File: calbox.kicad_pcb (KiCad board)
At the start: 2 copper layers, 101.6 x 76.2 mm, 80 parts, among them P1 BNC, P2 CONN_01X01, P3 CONN_01X01, Q1 Q_NPN_BEC, SW1 SW_Rotary12, SW2 SW_Rotary12, SW3 SW_SPDT, SW4 SW_Rotary12, SW5 SW_DPST_NKK_M2021, U1 74LVC161, U10 74LVC161, U11 74LVC74, U12 74LVC14, U13 LM317_SOT223_4pin, U14 LM317_SOT223_4pin, U2 74LVC161, U3 74LVC161, U4 74LVC161, U5 74LVC00, U6 74LVC161, U7 74LVC161, U8 74LVC00, U9 74LVC74, X1 ACHL_XO

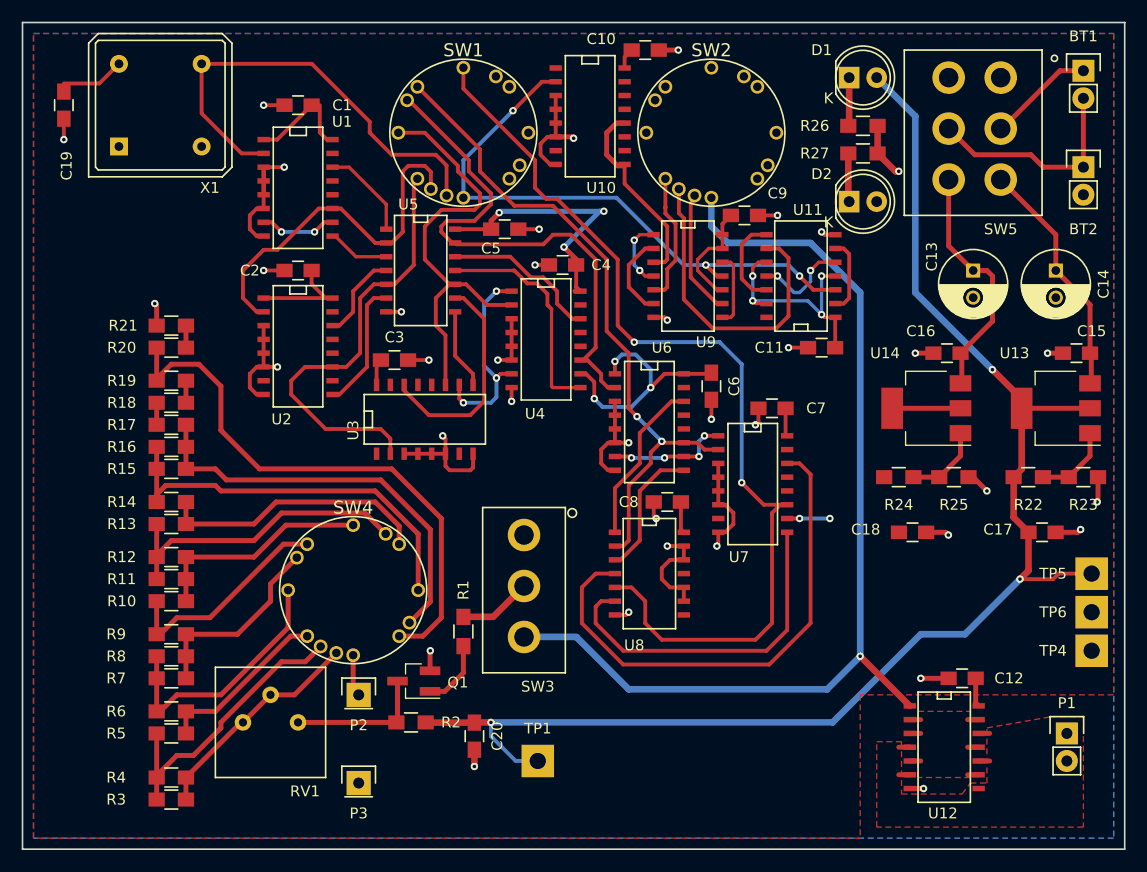
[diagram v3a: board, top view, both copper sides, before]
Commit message: R2 PCB rotary switches closer to middle of board
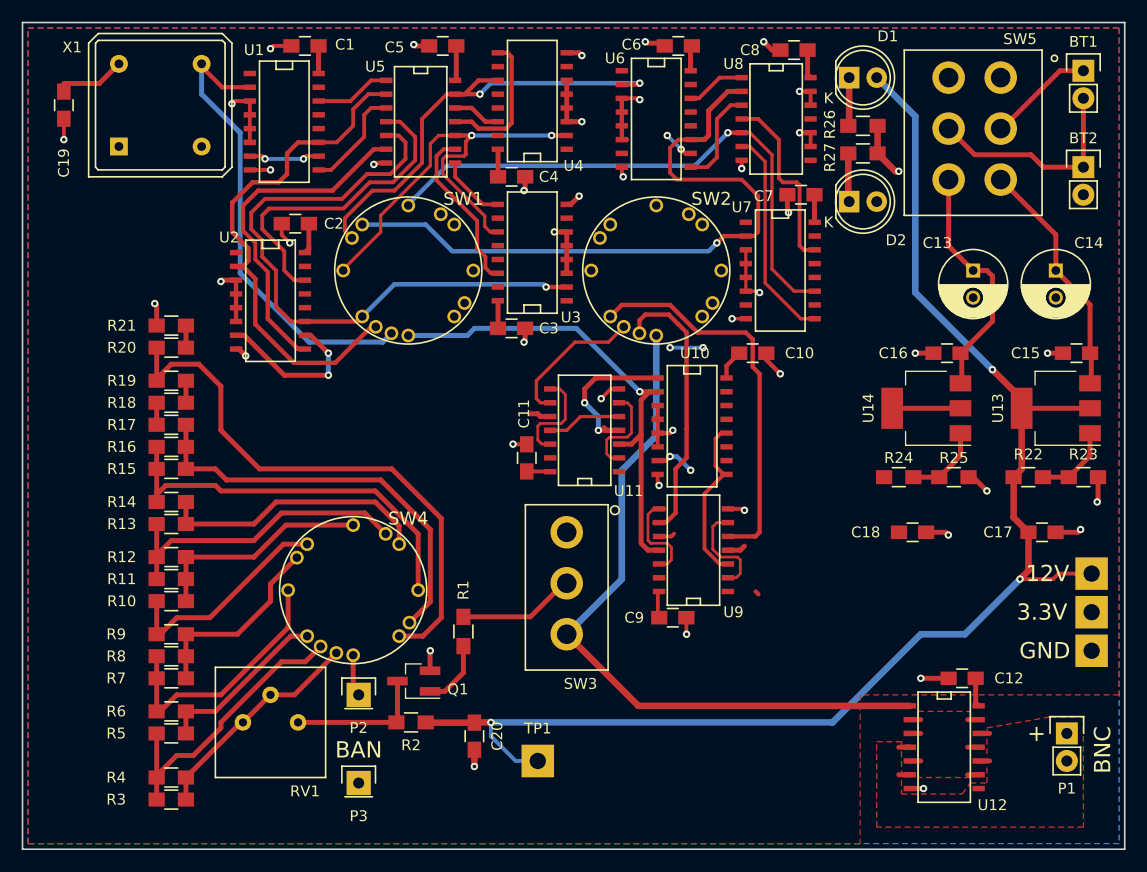
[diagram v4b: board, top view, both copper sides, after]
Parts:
- BT1, BT2: value Battery_Cell -> 9V_BATT
- D1, D2: value LED_ALT -> LED_GR
- P2: value CONN_01X01 -> BAN+
- P3: value CONN_01X01 -> BAN-
- Q1: value Q_NPN_BEC -> MMBT2369
- R17, R18, R19, R20, R21: value 100 -> 10
- R26: value R -> 470
- R27: value R -> 5
- SW1: value SW_Rotary12 -> FREQ SWITCH 1
- SW2: value SW_Rotary12 -> FREQ SWITCH 2
- SW3: value SW_SPDT -> PULSE/CONST
- SW4: value SW_Rotary12 -> VOLTAGE SWITCH
- SW5: value SW_DPST_NKK_M2021 -> POWER SWITCH
- TP4: value TEST -> GND
- TP5: value TEST -> 12V
- TP6: value TEST -> 3.3V
- U13, U14: value LM317_SOT223_4pin -> LM317
- X1: value ACHL_XO -> 20MHz
- moved U8 43.5 mm to (135.6, 95.2)
- moved C8 43.3 mm to (137.2, 88.9)
- moved C9 37.7 mm to (126.0, 141.2)
- moved C6 31.5 mm to (126.5, 88.5), turned to 180 degrees
- moved U10 30.1 mm to (127.8, 123.6)
- moved C10 29.6 mm to (133.3, 116.8)
- moved C11 29.0 mm to (112.5, 126.5), turned to 90 degrees
- moved U6 27.9 mm to (124.5, 95.2)
- moved U9 25.3 mm to (127.8, 135.0), turned to 90 degrees
- moved U11 24.5 mm to (117.7, 124.0)
- moved U4 22.0 mm to (113.0, 93.6), turned to 90 degrees
- moved C7 19.9 mm to (137.8, 102.2)
- moved U7 19.8 mm to (135.9, 109.2)
- moved U3 18.3 mm to (113.0, 107.6), turned to 90 degrees
- moved C5 17.8 mm to (104.8, 88.5), turned to 180 degrees
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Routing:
- net VCC: track 170.8 -> 92.9 mm, vias 23 -> 10
- net /clock_decade_division/20Hz_clock: track 89.7 -> 52.6 mm, vias 2 -> 1
- net Net-(U7-Pad14): track 47.4 -> 17.1 mm
- net /clock_final_division/clock_final_division_out: track 93.1 -> 65.3 mm, vias 1 -> 0
- net GND: track 131.5 -> 104.5 mm, vias 37 -> 44
- net /clock_final_division/div_by_5_out: track 12.7 -> 36.0 mm
- net Net-(U2-Pad14): track 8.17 -> 30.3 mm
- net Net-(U2-Pad9): track 12.0 -> 31.4 mm
- net /clock_decade_division/200kHz_clock: track 40.5 -> 58.3 mm, vias 0 -> 1
- net /clock_final_division/div_by_2_out: track 29.6 -> 13.2 mm
- net /clock_final_division/div_by_1_out: track 11.6 -> 25.9 mm
- net /clock_decade_division/2MHz_clock: track 34.0 -> 48.0 mm
- net Net-(U7-Pad9): track 32.0 -> 19.9 mm
- net Net-(U4-Pad14): track 14.6 -> 4.46 mm
- net Net-(U6-Pad14): track 15.4 -> 5.49 mm
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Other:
- net class Default: clearance 0.2 -> 0.1524; trace_width 0.3048 -> 0.254
- net class clock: clearance 0.254 -> 0.2032; trace_width 0.3556 -> 0.3048
- net class power: clearance 0.2 -> 0.1778
- rule trace_clearance: 0.2 -> 0.1524
- board text added: "+"
- board text added: "12V"
- board text added: "3.3V"
- board text added: "BAN"
- board text added: "BNC"
- board text added: "GND"
- board text added: "SOLDER BNC+ TO 50 OHM"

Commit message: update switch models in library, rotate final clock division switch
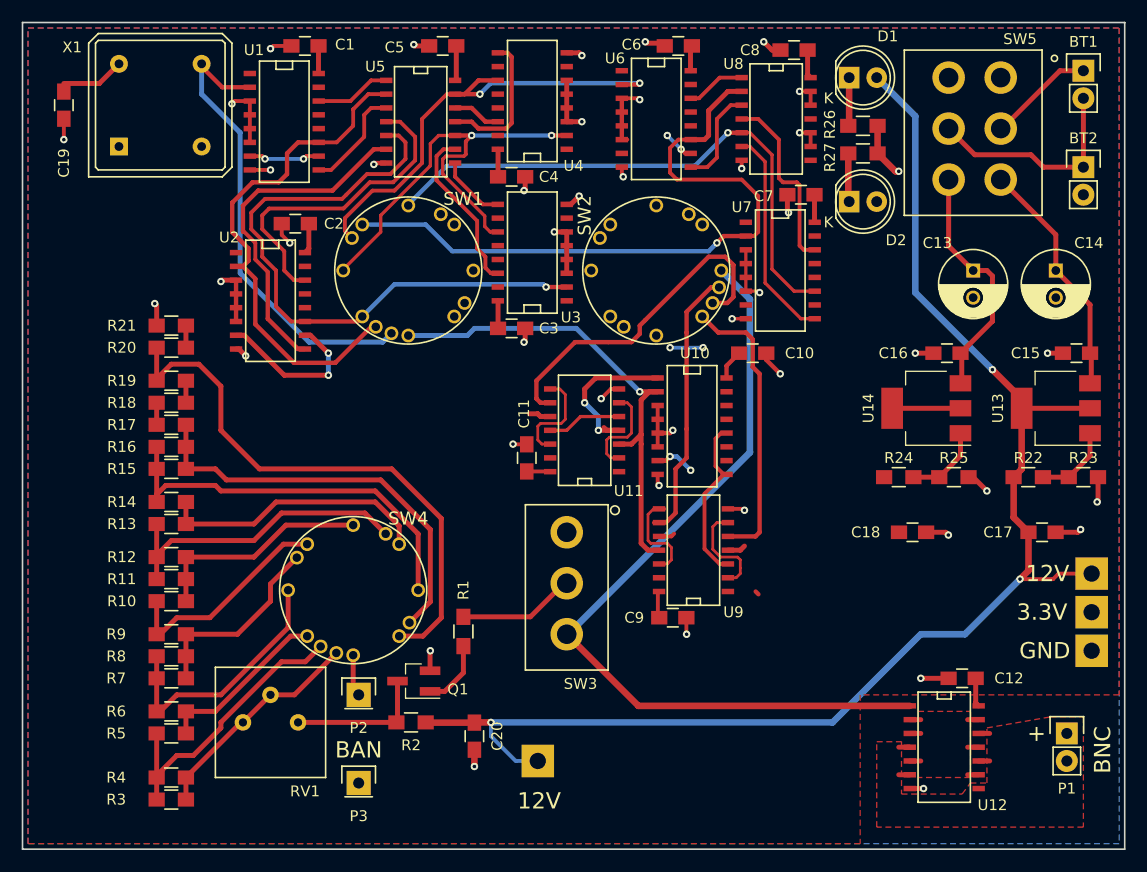
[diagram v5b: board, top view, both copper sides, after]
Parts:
- SW1: value FREQ SWITCH 1 -> ROTARY 7POS
- SW2: value FREQ SWITCH 2 -> ROTARY 3POS
- SW3: value PULSE/CONST -> SPDT
- SW4: value VOLTAGE SWITCH -> ROTARY 12POS
- SW5: value POWER SWITCH -> DPST
- TP1: value TEST -> 12V
- turned SW2 to 90 degrees
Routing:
- net /clock_final_division/div_by_2_out: track 13.2 -> 31.8 mm
- net /clock_final_division/clock_final_division_out: track 65.3 -> 76.1 mm
- net /clock_final_division/div_by_5_out: track 36.0 -> 26.6 mm
- net /clock_final_division/div_by_1_out: track 25.9 -> 25.3 mm
